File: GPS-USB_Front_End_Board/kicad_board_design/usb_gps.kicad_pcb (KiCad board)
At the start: 4 copper layers, 99.1 x 53.3 mm, 230 parts, among them J1 Micro-USB Connector, J3 SMA, P1 CONN_02X12, P2 CONN_01X03, U1 93LCxxB, U2 FT2232HL-REEL, U3 L4931 LDO, U4 MAX8510, U5 MAX8510, U6 MAX2771, U7 SAWTEK-855969, U8 LT1719S6 -- Not Populated, X1 13.368MHz TCXO, Y1 12MHz Crystal

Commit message: Final cleanup before submit to OSHPARK.
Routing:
- net GND: track 116.0 -> 125.6 mm, vias 37 -> 43
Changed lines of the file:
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@@
     (thickness 1.6)
     (drawings 6)
-    (tracks 916)
+    (tracks 938)
     (zones 0)
     (modules 230)
@@
     (0 F.Cu signal)
     (1 In1.Cu signal hide)
-    (2 In2.Cu signal hide)
+    (2 In2.Cu signal)
     (31 B.Cu signal hide)
     (32 B.Adhes user hide)
@@
   )
   (setup
-    (last_trace_width 0.254)
+    (last_trace_width 0.399999)
     (user_trace_width 0.254)
     (user_trace_width 0.399999)
@@
     (attr smd)
     (fp_text reference U1 (at -0.357089 -3.95345) (layer F.SilkS)
-      (effects (font (size 1.64685 1.64685) (thickness 0.05)))
+      (effects (font (size 1.64685 1.64685) (thickness 0.1524)))
     )
     (fp_text value 93LCxxB (at -0.356793 3.87371) (layer F.SilkS)
@@
     (at 86.868 73.406 270)
     (descr http://portal.fciconnect.com/Comergent//fci/drawing/10118194.pdf)
-    (fp_text reference J1 (at 0 -2.5 270) (layer F.SilkS)
+    (fp_text reference J1 (at 5.4864 1.3716 360) (layer F.SilkS)
       (effects (font (size 1 1) (thickness 0.15)))
     )
@@
   (via (at 133.1722 71.3359) (size 0.4572) (drill 0.254) (layers F.Cu B.Cu) (net 0))
   (segment (start 152.781 75.311) (end 152.908 75.311) (width 0.399999) (layer In1.Cu) (net 0))
+  (segment (start 133.689 80.01) (end 132.8166 80.01) (width 0.399999) (layer F.Cu) (net 1) (status 400000))
+  (segment (start 132.715 80.1116) (end 132.715 80.01) (width 0.399999) (layer In1.Cu) (net 1))
+  (via (at 132.715 80.1116) (size 0.4572) (drill 0.254) (layers F.Cu B.Cu) (net 1))
+  (segment (start 132.8166 80.01) (end 132.715 80.1116) (width 0.399999) (layer F.Cu) (net 1))
+  (segment (start 134.767 74.93) (end 133.3246 74.93) (width 0.399999) (layer F.Cu) (net 1) (status 400000))
+  (via (at 133.223 75.0316) (size 0.4572) (drill 0.254) (layers F.Cu B.Cu) (net 1))
+  (segment (start 133.3246 74.93) (end 133.223 75.0316) (width 0.399999) (layer F.Cu) (net 1))
+  (segment (start 106.51 102.87) (end 106.51 101.6586) (width 0.399999) (layer F.Cu) (net 1) (status 400000))
+  (via (at 106.5022 101.6508) (size 0.4572) (drill 0.254) (layers F.Cu B.Cu) (net 1))
+  (segment (start 106.51 101.6586) (end 106.5022 101.6508) (width 0.399999) (layer F.Cu) (net 1))
+  (segment (start 106.51 102.87) (end 107.6706 102.87) (width 0.399999) (layer F.Cu) (net 1) (status 400000))
+  (segment (start 107.7214 102.8192) (end 107.696 102.8446) (width 0.399999) (layer F.Cu) (net 1))
+  (segment (start 107.6706 102.87) (end 107.7214 102.8192) (width 0.399999) (layer F.Cu) (net 1))
+  (segment (start 103.59 99.06) (end 102.5144 99.06) (width 0.399999) (layer F.Cu) (net 1) (status 400000))
+  (via (at 102.489 99.0854) (size 0.4572) (drill 0.254) (layers F.Cu B.Cu) (net 1))
+  (segment (start 102.5144 99.06) (end 102.489 99.0854) (width 0.399999) (layer F.Cu) (net 1))
+  (segment (start 102.616 69.276) (end 103.7742 69.276) (width 0.399999) (layer F.Cu) (net 1) (status 400000))
+  (segment (start 103.8098 69.2404) (end 103.8606 69.2404) (width 0.399999) (layer In1.Cu) (net 1))
+  (via (at 103.8098 69.2404) (size 0.4572) (drill 0.254) (layers F.Cu B.Cu) (net 1))
+  (segment (start 103.7742 69.276) (end 103.8098 69.2404) (width 0.399999) (layer F.Cu) (net 1))
+  (segment (start 96.3549 93.4974) (end 98.3996 93.4974) (width 0.399999) (layer F.Cu) (net 1) (status 400000))
+  (via (at 98.3996 93.4974) (size 0.4572) (drill 0.254) (layers F.Cu B.Cu) (net 1))
   (segment (start 154.94 92.71) (end 155.5242 92.71) (width 0.399999) (layer In1.Cu) (net 1))
   (segment (start 98.445 102.235) (end 96.647 102.235) (width 0.399999) (layer F.Cu) (net 1))

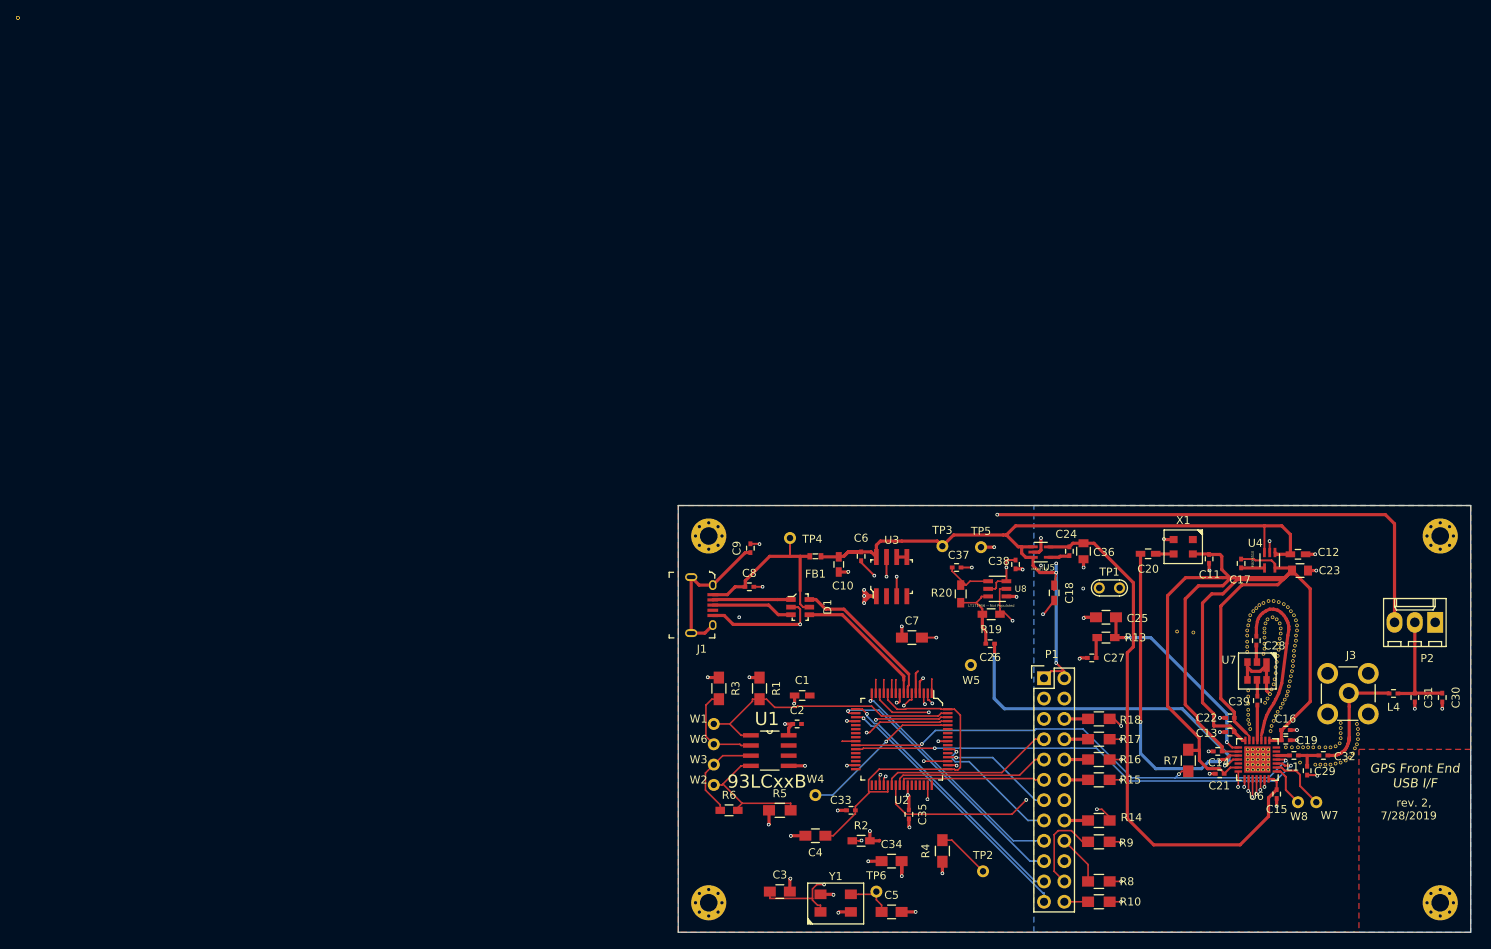
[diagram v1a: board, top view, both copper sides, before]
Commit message: Fix value display on EEPROM.  Consolidate some part values.
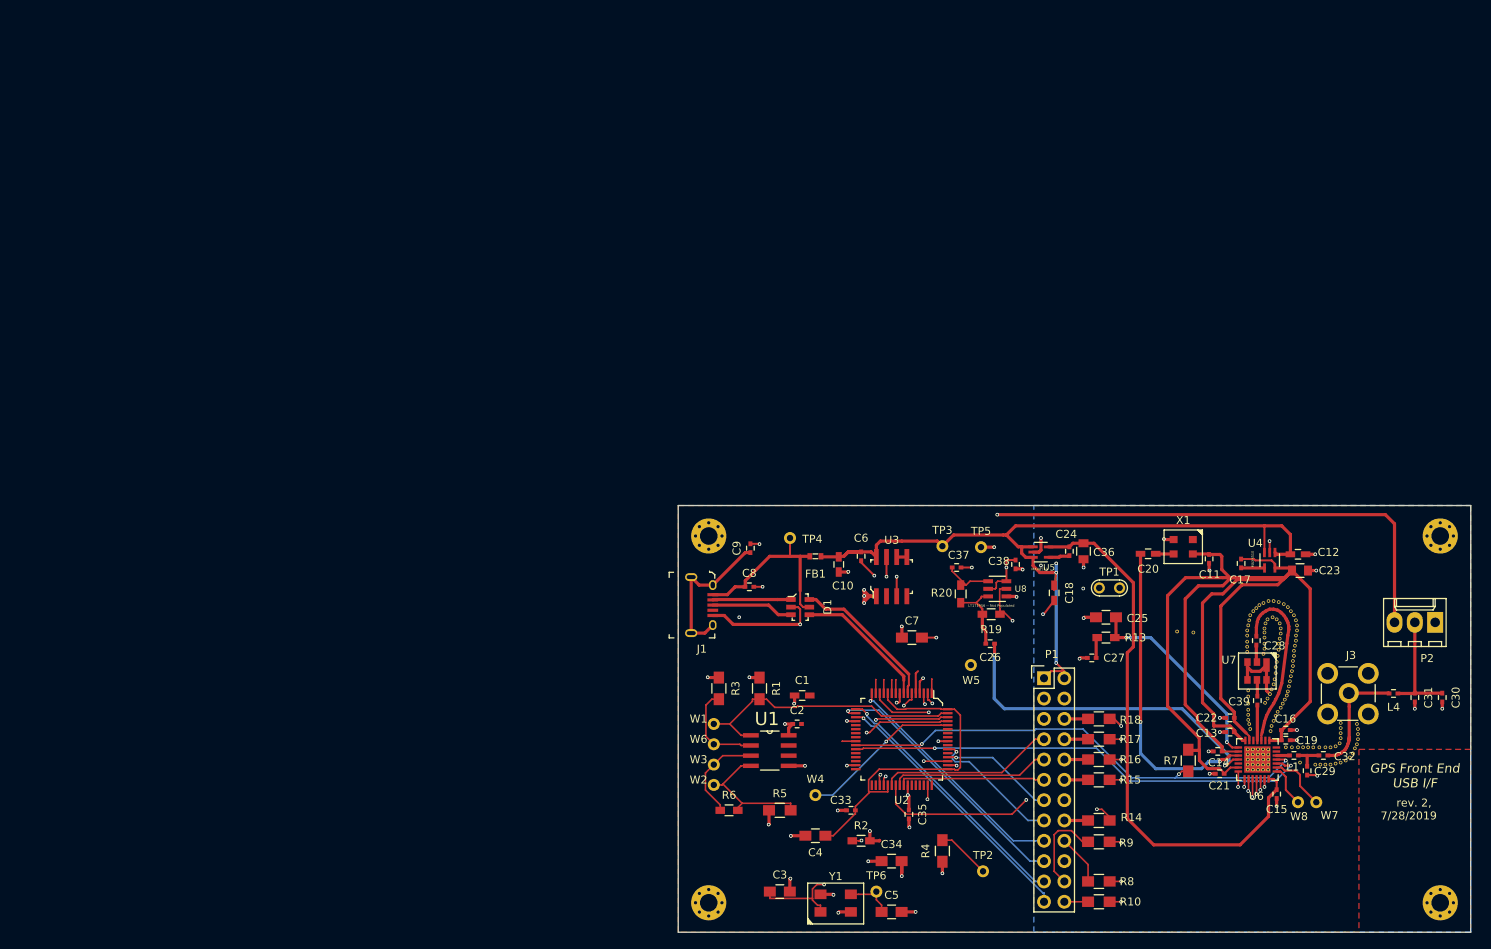
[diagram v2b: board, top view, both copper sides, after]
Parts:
- removed the REF** at (0.00, 0.00) (x2)
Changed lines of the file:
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@@
     (tracks 938)
     (zones 0)
-    (modules 230)
+    (modules 228)
     (nets 103)
   )
   (page A4)
   (layers
-    (0 F.Cu signal)
+    (0 F.Cu signal hide)
     (1 In1.Cu signal hide)
-    (2 In2.Cu signal)
+    (2 In2.Cu signal hide)
     (31 B.Cu signal hide)
     (32 B.Adhes user hide)
@@
       (net 1 GND) (zone_connect 2))
   )
-  (module via_10mil (layer F.Cu)
-    (at 0 0)
-    (fp_text reference REF** (at -0.15 0.95) (layer F.SilkS) hide
-      (effects (font (size 1 1) (thickness 0.15)))
-    )
-    (fp_text value via_10mil (at -0.05 -0.9) (layer F.Fab)
-      (effects (font (size 1 1) (thickness 0.15)))
-    )
-    (pad 1 thru_hole circle (at 0 0) (size 0.46 0.46) (drill 0.25) (layers *.Cu)
-      (zone_connect 2))
-  )
-  (module via_10mil (layer F.Cu)
-    (at 0 0)
-    (fp_text reference REF** (at -0.15 0.95) (layer F.SilkS) hide
-      (effects (font (size 1 1) (thickness 0.15)))
-    )
-    (fp_text value via_10mil (at -0.05 -0.9) (layer F.Fab) hide
-      (effects (font (size 1 1) (thickness 0.15)))
-    )
-    (pad 1 thru_hole circle (at 0 0) (size 0.46 0.46) (drill 0.25) (layers *.Cu)
-      (zone_connect 2))
-  )
   (module Capacitors_SMD:C_0603_HandSoldering (layer F.Cu)
     (at 98.044 84.709)
@@
       (effects (font (size 1.64685 1.64685) (thickness 0.1524)))
     )
-    (fp_text value 93LCxxB (at -0.356793 3.87371) (layer F.SilkS)
+    (fp_text value 93LCxxB (at -0.356793 3.87371) (layer F.SilkS) hide
       (effects (font (size 1.64548 1.64548) (thickness 0.05)))
     )
@@
   (via (at 133.1722 71.3359) (size 0.4572) (drill 0.254) (layers F.Cu B.Cu) (net 0))
   (segment (start 152.781 75.311) (end 152.908 75.311) (width 0.399999) (layer In1.Cu) (net 0))
-  (segment (start 133.689 80.01) (end 132.8166 80.01) (width 0.399999) (layer F.Cu) (net 1) (status 400000))
+  (segment (start 133.689 80.01) (end 132.8166 80.01) (width 0.399999) (layer F.Cu) (net 1))
   (segment (start 132.715 80.1116) (end 132.715 80.01) (width 0.399999) (layer In1.Cu) (net 1))
   (via (at 132.715 80.1116) (size 0.4572) (drill 0.254) (layers F.Cu B.Cu) (net 1))
   (segment (start 132.8166 80.01) (end 132.715 80.1116) (width 0.399999) (layer F.Cu) (net 1))
-  (segment (start 134.767 74.93) (end 133.3246 74.93) (width 0.399999) (layer F.Cu) (net 1) (status 400000))
+  (segment (start 134.767 74.93) (end 133.3246 74.93) (width 0.399999) (layer F.Cu) (net 1))
   (via (at 133.223 75.0316) (size 0.4572) (drill 0.254) (layers F.Cu B.Cu) (net 1))
   (segment (start 133.3246 74.93) (end 133.223 75.0316) (width 0.399999) (layer F.Cu) (net 1))
-  (segment (start 106.51 102.87) (end 106.51 101.6586) (width 0.399999) (layer F.Cu) (net 1) (status 400000))
+  (segment (start 106.51 102.87) (end 106.51 101.6586) (width 0.399999) (layer F.Cu) (net 1))
   (via (at 106.5022 101.6508) (size 0.4572) (drill 0.254) (layers F.Cu B.Cu) (net 1))
   (segment (start 106.51 101.6586) (end 106.5022 101.6508) (width 0.399999) (layer F.Cu) (net 1))
-  (segment (start 106.51 102.87) (end 107.6706 102.87) (width 0.399999) (layer F.Cu) (net 1) (status 400000))
+  (segment (start 106.51 102.87) (end 107.6706 102.87) (width 0.399999) (layer F.Cu) (net 1))
   (segment (start 107.7214 102.8192) (end 107.696 102.8446) (width 0.399999) (layer F.Cu) (net 1))
   (segment (start 107.6706 102.87) (end 107.7214 102.8192) (width 0.399999) (layer F.Cu) (net 1))
-  (segment (start 103.59 99.06) (end 102.5144 99.06) (width 0.399999) (layer F.Cu) (net 1) (status 400000))
+  (segment (start 103.59 99.06) (end 102.5144 99.06) (width 0.399999) (layer F.Cu) (net 1))
   (via (at 102.489 99.0854) (size 0.4572) (drill 0.254) (layers F.Cu B.Cu) (net 1))
   (segment (start 102.5144 99.06) (end 102.489 99.0854) (width 0.399999) (layer F.Cu) (net 1))
-  (segment (start 102.616 69.276) (end 103.7742 69.276) (width 0.399999) (layer F.Cu) (net 1) (status 400000))
+  (segment (start 102.616 69.276) (end 103.7742 69.276) (width 0.399999) (layer F.Cu) (net 1))
   (segment (start 103.8098 69.2404) (end 103.8606 69.2404) (width 0.399999) (layer In1.Cu) (net 1))
   (via (at 103.8098 69.2404) (size 0.4572) (drill 0.254) (layers F.Cu B.Cu) (net 1))
   (segment (start 103.7742 69.276) (end 103.8098 69.2404) (width 0.399999) (layer F.Cu) (net 1))
-  (segment (start 96.3549 93.4974) (end 98.3996 93.4974) (width 0.399999) (layer F.Cu) (net 1) (status 400000))
+  (segment (start 96.3549 93.4974) (end 98.3996 93.4974) (width 0.399999) (layer F.Cu) (net 1))
   (via (at 98.3996 93.4974) (size 0.4572) (drill 0.254) (layers F.Cu B.Cu) (net 1))
   (segment (start 154.94 92.71) (end 155.5242 92.71) (width 0.399999) (layer In1.Cu) (net 1))
@@
     (connect_pads (clearance 0.254))
     (min_thickness 0.254)
-    (fill (arc_segments 16) (thermal_gap 0.508) (thermal_bridge_width 0.508) (smoothing fillet) (radius 2.54))
+    (fill yes (arc_segments 16) (thermal_gap 0.508) (thermal_bridge_width 0.508) (smoothing fillet) (radius 2.54))
     (polygon
       (pts
